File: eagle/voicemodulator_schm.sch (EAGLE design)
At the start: 33 parts, among them T1 2N5089, T2 2N5089, T3 2N5089, T4 2N5089

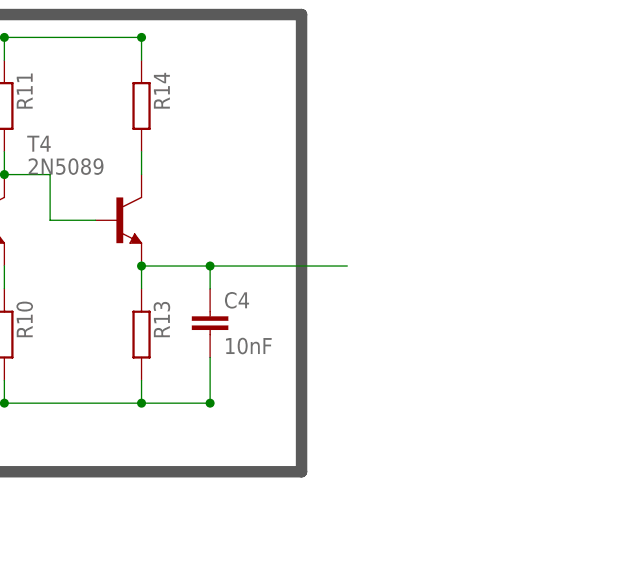
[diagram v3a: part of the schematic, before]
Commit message: Added output mic jack.
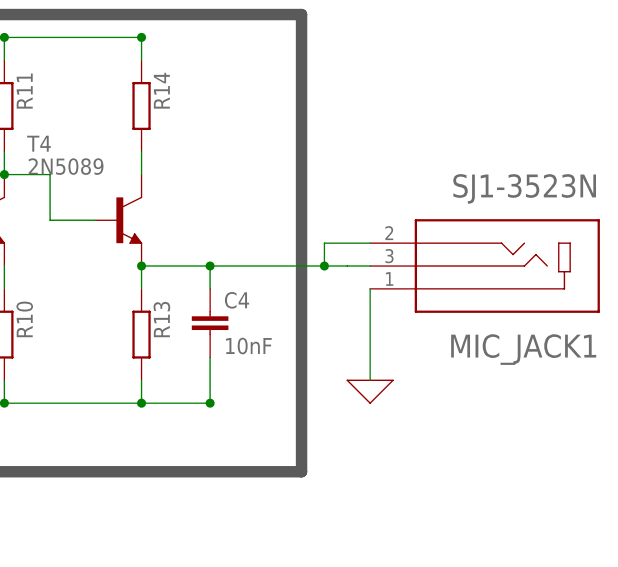
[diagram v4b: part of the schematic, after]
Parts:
- added MIC_JACK1: SJ1-3523N, SJ1-3523N:SJ1-3523N
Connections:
- net 0: now also MIC_JACK1.1
- net N$11: now also MIC_JACK1.2, MIC_JACK1.3
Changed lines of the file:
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@@
 <part name="LED2" library="led" library_urn="urn:adsk.eagle:library:259" deviceset="LED" device="10MM" package3d_urn="urn:adsk.eagle:package:15828/1"/>
 <part name="LED3" library="led" library_urn="urn:adsk.eagle:library:259" deviceset="LED" device="10MM" package3d_urn="urn:adsk.eagle:package:15828/1"/>
+<part name="MIC_JACK1" library="SJ1-3523N" deviceset="SJ1-3523N" device=""/>
+<part name="X_3" library="ngspice-simulation" library_urn="urn:adsk.eagle:library:527439" deviceset="GND" device=""/>
 </parts>
 <sheets>
@@
 <attribute name="VALUE" x="-40.005" y="30.988" size="1.778" layer="96" rot="R90"/>
 </instance>
+<instance part="MIC_JACK1" gate="G$1" x="182.88" y="5.08" rot="R180">
+<attribute name="NAME" x="193.0489" y="-2.54665" size="2.54221875" layer="95" rot="R180"/>
+<attribute name="VALUE" x="193.0453" y="15.2453" size="2.541340625" layer="96" rot="R180"/>
+</instance>
+<instance part="X_3" gate="G$1" x="167.64" y="-7.62"/>
 </instances>
 <busses>
@@
 <junction x="48.26" y="7.62"/>
 </segment>
+<segment>
+<pinref part="MIC_JACK1" gate="G$1" pin="1"/>
+<pinref part="X_3" gate="G$1" pin="0"/>
+<wire x1="167.64" y1="2.54" x2="167.64" y2="-7.62" width="0.1524" layer="91"/>
+</segment>
 </net>
 <net name="N$1" class="0">
@@
 <wire x1="149.86" y1="2.54" x2="149.86" y2="5.08" width="0.1524" layer="91"/>
 <wire x1="149.86" y1="5.08" x2="142.24" y2="5.08" width="0.1524" layer="91"/>
-<wire x1="149.86" y1="5.08" x2="165.1" y2="5.08" width="0.127" layer="91"/>
+<wire x1="149.86" y1="5.08" x2="162.56" y2="5.08" width="0.127" layer="91"/>
 <junction x="149.86" y="5.08"/>
 <junction x="142.24" y="5.08"/>
-</segment>
-</net>
+<pinref part="MIC_JACK1" gate="G$1" pin="3"/>
+<wire x1="162.56" y1="5.08" x2="165.1" y2="5.08" width="0.127" layer="91"/>
+<wire x1="167.64" y1="5.08" x2="165.1" y2="5.08" width="0.1524" layer="91"/>
+<pinref part="MIC_JACK1" gate="G$1" pin="2"/>
+<wire x1="162.56" y1="5.08" x2="162.56" y2="7.62" width="0.1524" layer="91"/>
+<wire x1="162.56" y1="7.62" x2="167.64" y2="7.62" width="0.1524" layer="91"/>
+<junction x="162.56" y="5.08"/>
+</segment>
+</net>

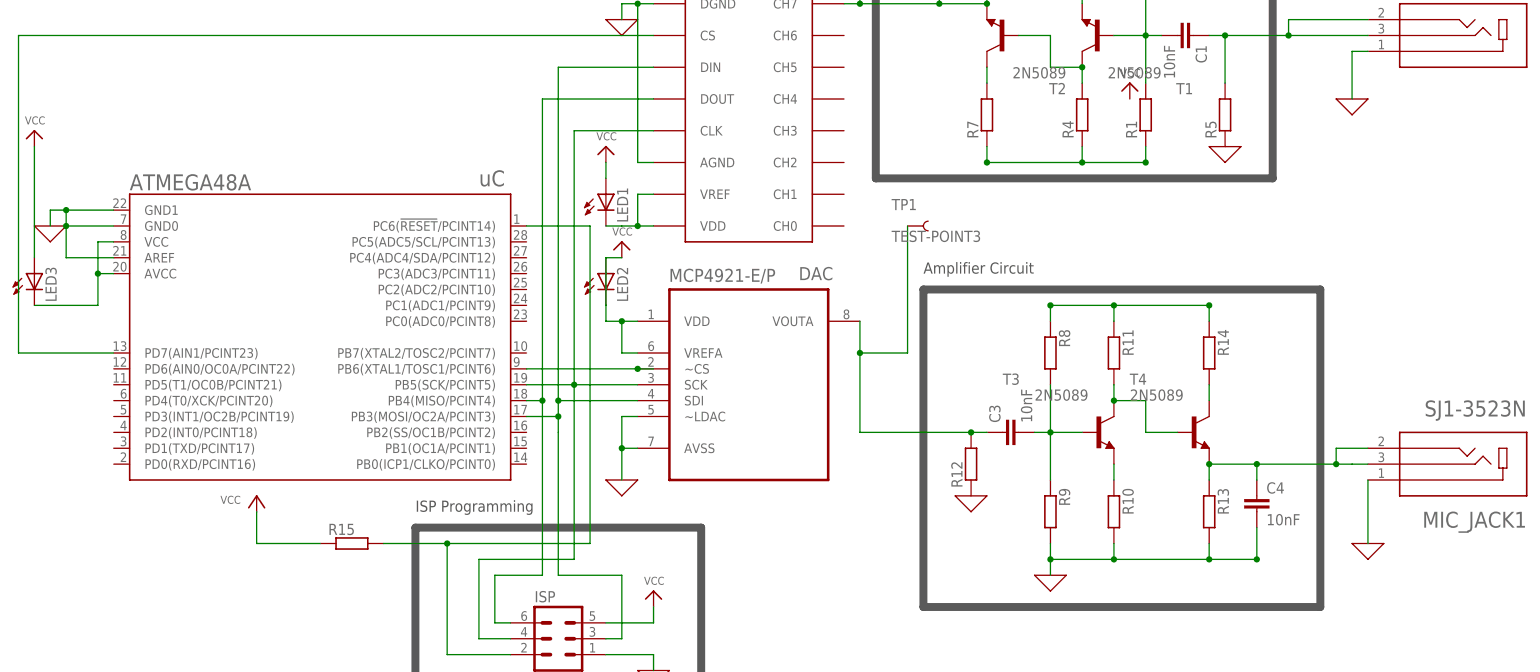
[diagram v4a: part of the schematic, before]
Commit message: Fix incorrect dimensions in eagle library for DIP
48A DIP device dimensions on layout were incorrect and needed modifying
to match what is specified in the datasheet.
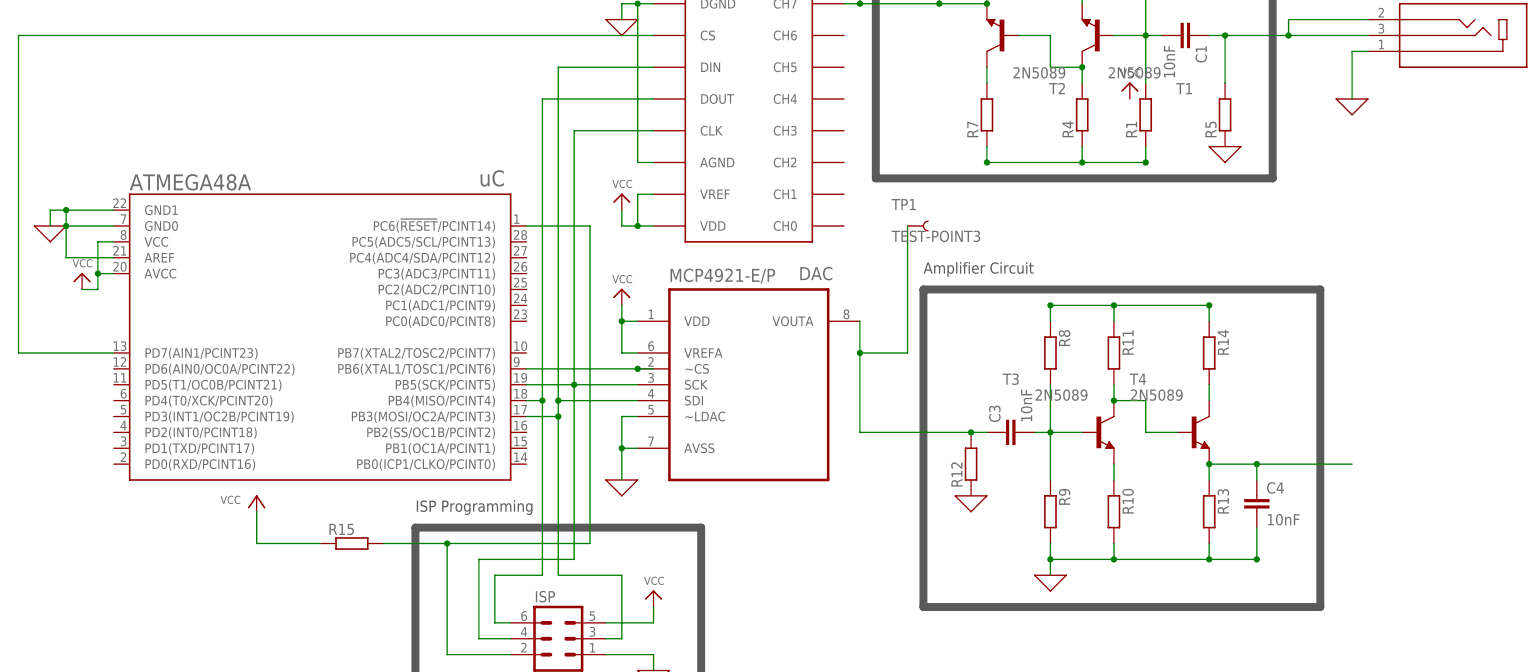
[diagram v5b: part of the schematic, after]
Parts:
- removed LED1, LED2, LED3: (no value), led:LED10MM
- removed MIC_JACK1: SJ1-3523N, SJ1-3523N:SJ1-3523N
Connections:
- removed net N$18: ADC.VDD, ADC.VREF, LED1.C
- removed net N$21: ATMEGA48A.AVCC, ATMEGA48A.VCC, LED3.C
- net 0: no longer MIC_JACK1.1
- net N$11: no longer MIC_JACK1.2, MIC_JACK1.3
- net VCC: now also ADC.VDD, ADC.VREF, ATMEGA48A.AVCC, ATMEGA48A.VCC; no longer LED1.A, LED2.A, LED2.C, LED3.A

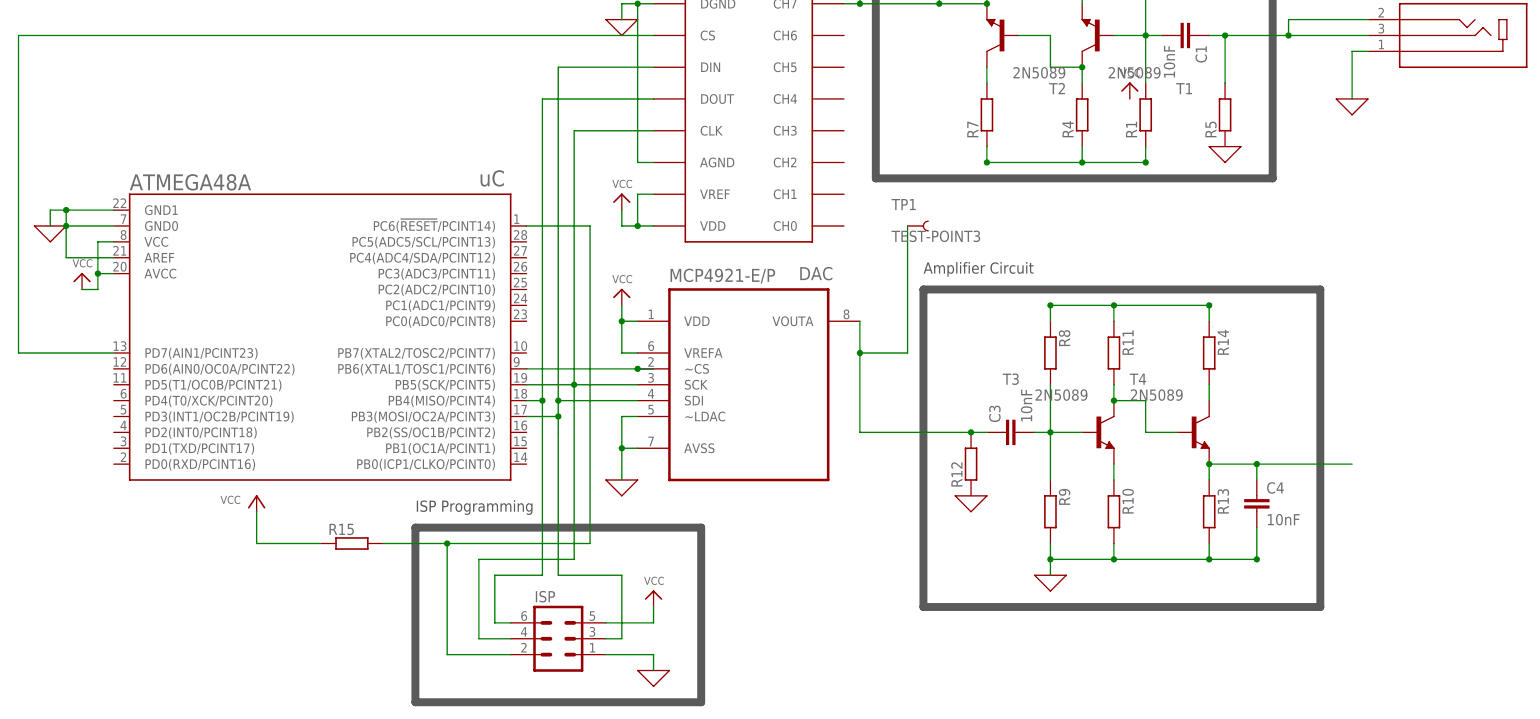
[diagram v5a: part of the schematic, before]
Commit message: Segmented output into two paths with 0 ohm resistors
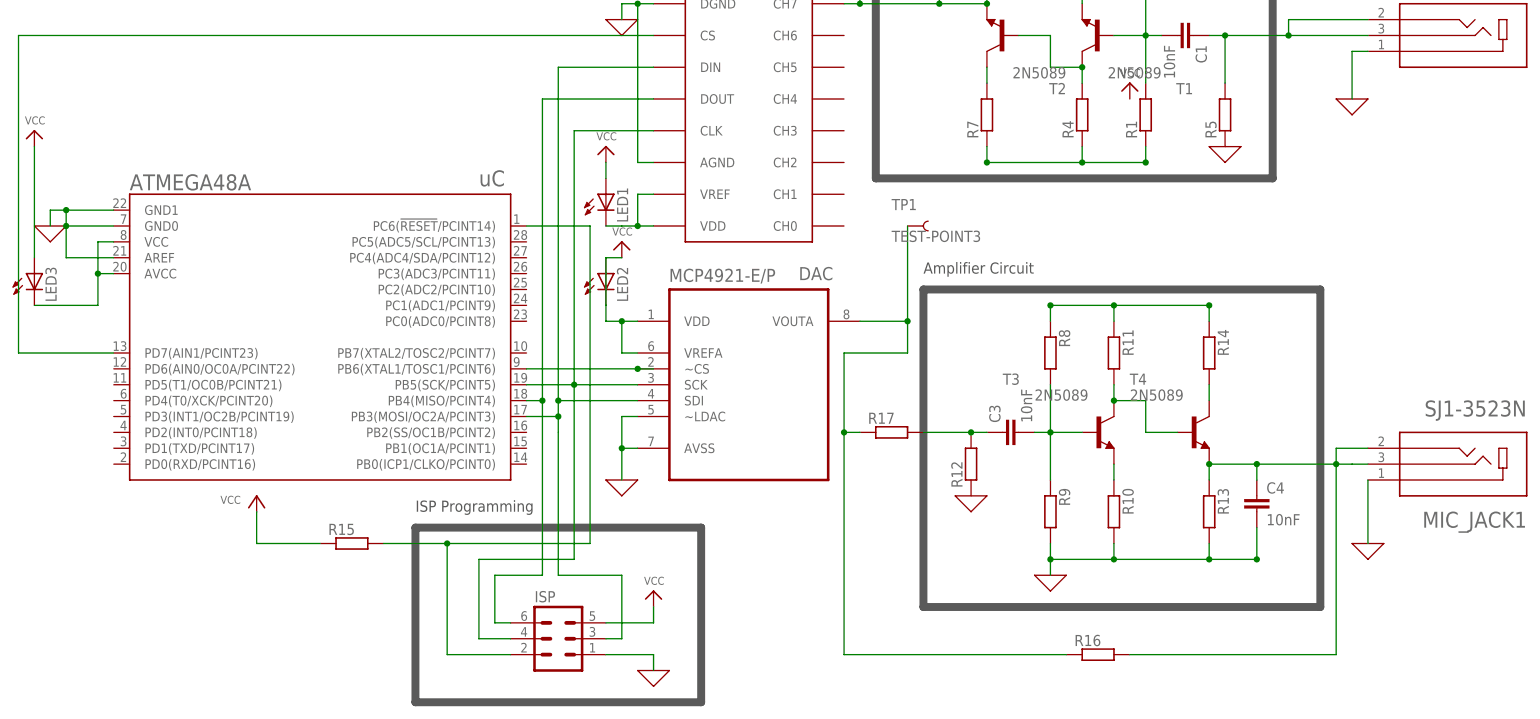
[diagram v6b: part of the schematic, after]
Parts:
- added LED1, LED2, LED3: (no value), led:LED10MM
- added MIC_JACK1: SJ1-3523N, SJ1-3523N:SJ1-3523N
- added R16, R17: (no value), resistor-shunt:SMR-WAV
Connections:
- new net N$18: ADC.VDD, ADC.VREF, LED1.C
- new net N$21: ATMEGA48A.AVCC, ATMEGA48A.VCC, LED3.C
- new net N$23: C3.1, R12.1, R17.1
- net 0: now also MIC_JACK1.1
- net N$11: now also MIC_JACK1.2, MIC_JACK1.3, R16.1
- net N$4: now also R16.2, R17.2; no longer C3.1, R12.1
- net VCC: now also LED1.A, LED2.A, LED2.C, LED3.A; no longer ADC.VDD, ADC.VREF, ATMEGA48A.AVCC, ATMEGA48A.VCC

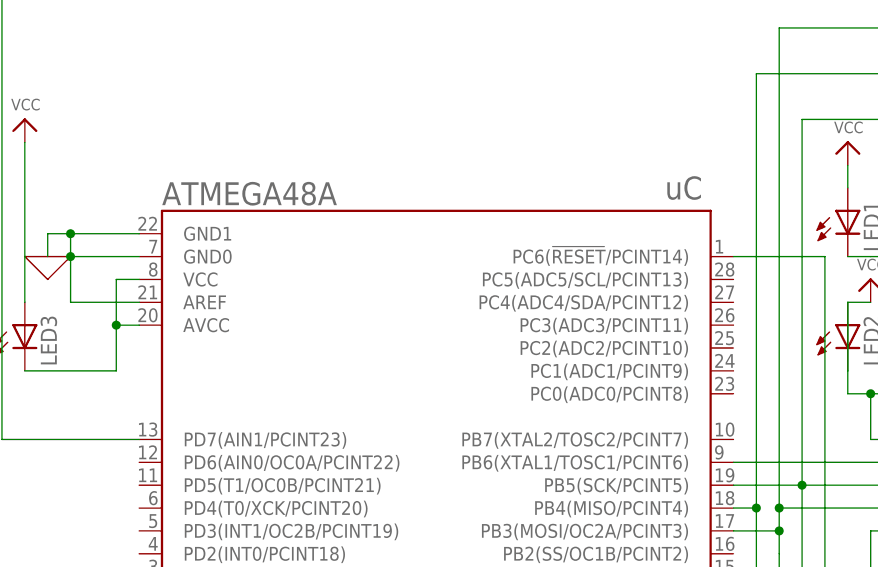
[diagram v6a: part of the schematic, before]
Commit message: Updated with new model that is adjusted to correct Atmega48A dimensions.
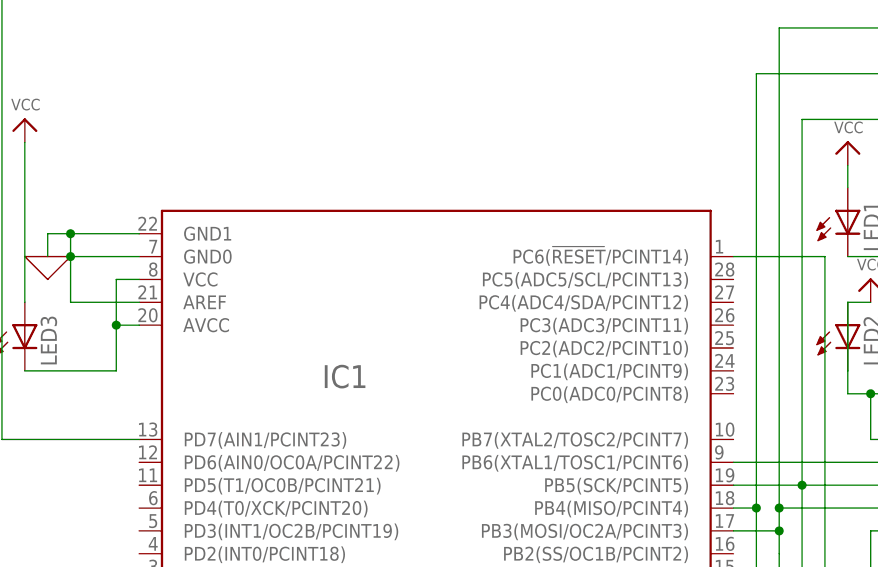
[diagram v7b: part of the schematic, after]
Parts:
- removed ATMEGA48A: uC, ece411_fixes:ATMEGA48/88/168/328-PU(DIP28)PU
- added IC1: (no value), voicemod_parts:ATMEGA48/88/168/328-PU(DIP28)PU
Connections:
- net 0: now also IC1.AREF, IC1.GND0, IC1.GND1; no longer ATMEGA48A.AREF, ATMEGA48A.GND0, ATMEGA48A.GND1
- net N$16: now also IC1.PB3(MOSI/OC2A/PCINT3); no longer ATMEGA48A.PB3(MOSI/OC2A/PCINT3)
- net N$17: now also IC1.PB5(SCK/PCINT5); no longer ATMEGA48A.PB5(SCK/PCINT5)
- net N$19: now also IC1.PD7(AIN1/PCINT23); no longer ATMEGA48A.PD7(AIN1/PCINT23)
- net N$2: now also IC1.PB4(MISO/PCINT4); no longer ATMEGA48A.PB4(MISO/PCINT4)
- net N$20: now also IC1.PB6(XTAL1/TOSC1/PCINT6); no longer ATMEGA48A.PB6(XTAL1/TOSC1/PCINT6)
- net N$21: now also IC1.AVCC, IC1.VCC; no longer ATMEGA48A.AVCC, ATMEGA48A.VCC
- net N$22: now also IC1.PC6(!RESET!/PCINT14); no longer ATMEGA48A.PC6(!RESET!/PCINT14)
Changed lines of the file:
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@@
 <part name="X_10" library="ngspice-simulation" library_urn="urn:adsk.eagle:library:527439" deviceset="GND" device=""/>
 <part name="P+6" library="audio amplifier example" library_urn="urn:adsk.eagle:library:970892" deviceset="VCC" device=""/>
-<part name="ATMEGA48A" library="ece411_fixes" deviceset="ATMEGA48/88/168/328-PU(DIP28)" device="PU" value="uC"/>
 <part name="DAC" library="Microchip_By_element14_Batch_1" deviceset="MCP4921-E/P" device=""/>
 <part name="TP1" library="SparkFun-Connectors" library_urn="urn:adsk.eagle:library:513" deviceset="TEST-POINT" device="3" package3d_urn="urn:adsk.eagle:package:38286/1"/>
@@
 <part name="R16" library="resistor-shunt" library_urn="urn:adsk.eagle:library:346" deviceset="SMR-WAV" device="" package3d_urn="urn:adsk.eagle:package:25223/1"/>
 <part name="R17" library="resistor-shunt" library_urn="urn:adsk.eagle:library:346" deviceset="SMR-WAV" device="" package3d_urn="urn:adsk.eagle:package:25223/1"/>
+<part name="IC1" library="voicemod_parts" deviceset="ATMEGA48/88/168/328-PU(DIP28)" device="PU"/>
 </parts>
 <sheets>
@@
 <attribute name="VALUE" x="51.816" y="-14.224" size="1.27" layer="96"/>
 </instance>
-<instance part="ATMEGA48A" gate="IC" x="0" y="25.4" rot="R180">
-<attribute name="NAME" x="-30.48" y="48.895" size="2.54" layer="95" ratio="12"/>
-<attribute name="VALUE" x="25.4" y="49.53" size="2.54" layer="96" ratio="12"/>
-</instance>
 <instance part="DAC" gate="A" x="68.58" y="20.32">
 <attribute name="NAME" x="76.5556" y="34.5186" size="2.0828" layer="95" ratio="10" rot="SR0"/>
@@
 <attribute name="NAME" x="87.63" y="11.5316" size="1.778" layer="95"/>
 <attribute name="VALUE" x="87.63" y="7.239" size="1.778" layer="96"/>
+</instance>
+<instance part="IC1" gate="IC" x="0" y="25.4" rot="R180">
+<attribute name="NAME" x="-12.7" y="28.575" size="2.54" layer="95" ratio="12"/>
+<attribute name="VALUE" x="-12.7" y="31.75" size="2.54" layer="96" ratio="12"/>
 </instance>
 </instances>
@@
 </segment>
 <segment>
-<pinref part="ATMEGA48A" gate="IC" pin="GND1"/>
 <wire x1="-33.02" y1="45.72" x2="-40.64" y2="45.72" width="0.1524" layer="91"/>
 <pinref part="X_9" gate="G$1" pin="0"/>
 <wire x1="-40.64" y1="45.72" x2="-43.18" y2="45.72" width="0.1524" layer="91"/>
 <wire x1="-43.18" y1="45.72" x2="-43.18" y2="43.18" width="0.1524" layer="91"/>
-<pinref part="ATMEGA48A" gate="IC" pin="AREF"/>
 <wire x1="-33.02" y1="38.1" x2="-40.64" y2="38.1" width="0.1524" layer="91"/>
 <wire x1="-40.64" y1="38.1" x2="-40.64" y2="43.18" width="0.1524" layer="91"/>
-<pinref part="ATMEGA48A" gate="IC" pin="GND0"/>
 <wire x1="-40.64" y1="45.72" x2="-40.64" y2="43.18" width="0.1524" layer="91"/>
 <wire x1="-40.64" y1="43.18" x2="-33.02" y2="43.18" width="0.1524" layer="91"/>
 <junction x="-40.64" y="43.18"/>
 <junction x="-40.64" y="45.72"/>
+<pinref part="IC1" gate="IC" pin="AREF"/>
+<pinref part="IC1" gate="IC" pin="GND0"/>
+<pinref part="IC1" gate="IC" pin="GND1"/>
 </segment>
 <segment>
@@
 <wire x1="27.94" y1="-20.32" x2="30.48" y2="-20.32" width="0.1524" layer="91"/>
 <junction x="35.56" y="15.24"/>
-<pinref part="ATMEGA48A" gate="IC" pin="PB4(MISO/PCINT4)"/>
+<pinref part="IC1" gate="IC" pin="PB4(MISO/PCINT4)"/>
 </segment>
 </net>
@@
 <pinref part="ISP" gate="1" pin="3"/>
 <wire x1="48.26" y1="-22.86" x2="45.72" y2="-22.86" width="0.1524" layer="91"/>
-<pinref part="ATMEGA48A" gate="IC" pin="PB3(MOSI/OC2A/PCINT3)"/>
 <pinref part="DAC" gate="A" pin="SDI"/>
 <wire x1="50.8" y1="15.24" x2="38.1" y2="15.24" width="0.1524" layer="91"/>
 <junction x="38.1" y="15.24"/>
+<pinref part="IC1" gate="IC" pin="PB3(MOSI/OC2A/PCINT3)"/>
 </segment>
 </net>
@@
 <pinref part="ISP" gate="1" pin="4"/>
 <wire x1="25.4" y1="-22.86" x2="30.48" y2="-22.86" width="0.1524" layer="91"/>
-<pinref part="ATMEGA48A" gate="IC" pin="PB5(SCK/PCINT5)"/>
 <pinref part="DAC" gate="A" pin="SCK"/>
 <wire x1="50.8" y1="17.78" x2="40.64" y2="17.78" width="0.1524" layer="91"/>
+<pinref part="IC1" gate="IC" pin="PB5(SCK/PCINT5)"/>
 </segment>
 </net>
@@
 <wire x1="-48.26" y1="73.66" x2="-48.26" y2="22.86" width="0.127" layer="91"/>
 <wire x1="-48.26" y1="22.86" x2="-33.02" y2="22.86" width="0.127" layer="91"/>
-<pinref part="ATMEGA48A" gate="IC" pin="PD7(AIN1/PCINT23)"/>
+<pinref part="IC1" gate="IC" pin="PD7(AIN1/PCINT23)"/>
 </segment>
 </net>
@@
 <segment>
 <wire x1="33.02" y1="20.32" x2="50.8" y2="20.32" width="0.127" layer="91"/>
-<pinref part="ATMEGA48A" gate="IC" pin="PB6(XTAL1/TOSC1/PCINT6)"/>
 <pinref part="DAC" gate="A" pin="~CS"/>
 <wire x1="50.8" y1="20.32" x2="53.34" y2="20.32" width="0.127" layer="91"/>
 <junction x="50.8" y="20.32"/>
+<pinref part="IC1" gate="IC" pin="PB6(XTAL1/TOSC1/PCINT6)"/>
 </segment>
 </net>
@@
 <pinref part="ISP" gate="1" pin="2"/>
 <wire x1="20.32" y1="-25.4" x2="30.48" y2="-25.4" width="0.1524" layer="91"/>
-<pinref part="ATMEGA48A" gate="IC" pin="PC6(!RESET!/PCINT14)"/>
 <pinref part="R15" gate="G$1" pin="1"/>
 <wire x1="20.32" y1="-7.62" x2="10.16" y2="-7.62" width="0.1524" layer="91"/>
 <junction x="20.32" y="-7.62"/>
+<pinref part="IC1" gate="IC" pin="PC6(!RESET!/PCINT14)"/>
 </segment>
 </net>
@@
 <net name="N$21" class="0">
 <segment>
-<pinref part="ATMEGA48A" gate="IC" pin="VCC"/>
 <wire x1="-33.02" y1="40.64" x2="-35.56" y2="40.64" width="0.1524" layer="91"/>
 <wire x1="-35.56" y1="40.64" x2="-35.56" y2="35.56" width="0.1524" layer="91"/>
-<pinref part="ATMEGA48A" gate="IC" pin="AVCC"/>
 <wire x1="-33.02" y1="35.56" x2="-35.56" y2="35.56" width="0.1524" layer="91"/>
 <junction x="-35.56" y="35.56"/>
@@
 <wire x1="-45.72" y1="30.48" x2="-35.56" y2="30.48" width="0.1524" layer="91"/>
 <wire x1="-35.56" y1="30.48" x2="-35.56" y2="35.56" width="0.1524" layer="91"/>
-</segment>
-</net>
+<pinref part="IC1" gate="IC" pin="AVCC"/>
+<pinref part="IC1" gate="IC" pin="VCC"/>
+</segment>
+</net>
